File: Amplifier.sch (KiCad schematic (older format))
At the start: 49 parts, among them J501 Screw_Terminal_01x04, SW501 SW_DIP_x02, U501 TDA7498L

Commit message: fast alle footprints herausgesucht. Spulen typen rausgesucht: Bourns spulen
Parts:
- removed C525: 560uF 50V, Capacitor_THT:CP_Radial_D12.5mm_P5.00mm, symbol Device:CP
- added C530, C531, C532: 560uF 50V, Capacitor_THT:CP_Radial_D12.5mm_P5.00mm, symbol Device:CP_Small
- C525: renamed from C?; footprint (none) -> Capacitor_THT:CP_Radial_D13.0mm_P5.00mm
- C526, C527, C528, C529: footprint (none) -> Capacitor_SMD:C_0603_1608Metric_Pad1.05x0.95mm_HandSolder
- J501: value Screw_Terminal_01x04 -> TB001-500-04BE CUI_Devices; footprint (none) -> TerminalBlock_RND:TerminalBlock_RND_205-00047_1x04_P5.00mm_Horizontal
- L501, L502, L503, L504: value 22uH -> 22uH 6100-220K-RC
- R501, R502, R503, R504, R505, R512: footprint (none) -> Resistor_SMD:R_0603_1608Metric_Pad1.05x0.95mm_HandSolder
- R506, R507, R508, R509, R510, R511: footprint (none) -> Resistor_SMD:R_1206_3216Metric_Pad1.42x1.75mm_HandSolder
- SW501: value SW_DIP_x02 -> DS04-254-2-02BK-SMT; footprint (none) -> Package_DIP:DIP-4_W8.89mm_SMDSocket_LongPads
- U501: footprint (none) -> Package_SO:ST_PowerSSO-36_SlugDown_ThermalVias
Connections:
- net GNDPWR: now also C525.2, C530.2, C531.2, C532.2
- net POWER_AMP: now also C511.2, C512.1, C514.2, C515.1, C525.1, U501.12 (PVCCA), U501.13 (PVCCA), U501.6 (PVCCB), U501.7 (PVCCB), C530.1, C531.1, C532.1
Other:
- moved on the sheet: C525
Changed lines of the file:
@@
 F 0 "U501" H 5425 5415 50  0000 C CNN
 F 1 "TDA7498L" H 5425 5324 50  0000 C CNN
-F 2 "" H 5550 4250 50  0001 C CNN
+F 2 "Package_SO:ST_PowerSSO-36_SlugDown_ThermalVias" H 5550 4250 50  0001 C CNN
 F 3 "" H 5550 4250 50  0001 C CNN
 	1    5400 3650
@@
 F 0 "R506" H 6959 2446 50  0000 L CNN
 F 1 "22R" H 6959 2355 50  0000 L CNN
-F 2 "" H 6900 2400 50  0001 C CNN
+F 2 "Resistor_SMD:R_1206_3216Metric_Pad1.42x1.75mm_HandSolder" H 6900 2400 50  0001 C CNN
 F 3 "~" H 6900 2400 50  0001 C CNN
 	1    6900 2400
@@
 P 7300 2150
 F 0 "L501" V 7505 2150 50  0000 C CNN
-F 1 "22uH" V 7414 2150 50  0000 C CNN
+F 1 "22uH 6100-220K-RC " V 7414 2150 50  0000 C CNN
 F 2 "" H 7300 2150 50  0001 C CNN
 F 3 "~" H 7300 2150 50  0001 C CNN
@@
 P 7300 3300
 F 0 "L502" V 7505 3300 50  0000 C CNN
-F 1 "22uH" V 7414 3300 50  0000 C CNN
+F 1 "22uH 6100-220K-RC " V 7414 3300 50  0000 C CNN
 F 2 "" H 7300 3300 50  0001 C CNN
 F 3 "~" H 7300 3300 50  0001 C CNN
@@
 F 0 "R509" H 8509 3196 50  0000 L CNN
 F 1 "8R" H 8509 3105 50  0000 L CNN
-F 2 "" H 8450 3150 50  0001 C CNN
+F 2 "Resistor_SMD:R_1206_3216Metric_Pad1.42x1.75mm_HandSolder" H 8450 3150 50  0001 C CNN
 F 3 "~" H 8450 3150 50  0001 C CNN
 	1    8450 3150
@@
 F 0 "C527" H 8542 2946 50  0000 L CNN
 F 1 "220nF" H 8542 2855 50  0000 L CNN
-F 2 "" H 8450 2900 50  0001 C CNN
+F 2 "Capacitor_SMD:C_0603_1608Metric_Pad1.05x0.95mm_HandSolder" H 8450 2900 50  0001 C CNN
 F 3 "~" H 8450 2900 50  0001 C CNN
 	1    8450 2900
@@
 F 0 "R508" H 8509 2346 50  0000 L CNN
 F 1 "8R" H 8509 2255 50  0000 L CNN
-F 2 "" H 8450 2300 50  0001 C CNN
+F 2 "Resistor_SMD:R_1206_3216Metric_Pad1.42x1.75mm_HandSolder" H 8450 2300 50  0001 C CNN
 F 3 "~" H 8450 2300 50  0001 C CNN
 	1    8450 2300
@@
 F 0 "C526" H 8542 2596 50  0000 L CNN
 F 1 "220nF" H 8542 2505 50  0000 L CNN
-F 2 "" H 8450 2550 50  0001 C CNN
+F 2 "Capacitor_SMD:C_0603_1608Metric_Pad1.05x0.95mm_HandSolder" H 8450 2550 50  0001 C CNN
 F 3 "~" H 8450 2550 50  0001 C CNN
 	1    8450 2550
@@
 P 10300 3650
 F 0 "J501" H 10380 3642 50  0000 L CNN
-F 1 "Screw_Terminal_01x04" H 10380 3551 50  0000 L CNN
-F 2 "" H 10300 3650 50  0001 C CNN
+F 1 "TB001-500-04BE CUI_Devices" H 10000 3300 50  0000 L CNN
+F 2 "TerminalBlock_RND:TerminalBlock_RND_205-00047_1x04_P5.00mm_Horizontal" H 10300 3650 50  0001 C CNN
 F 3 "~" H 10300 3650 50  0001 C CNN
 	1    10300 3650
@@
 F 0 "R507" H 6959 4296 50  0000 L CNN
 F 1 "22R" H 6959 4205 50  0000 L CNN
-F 2 "" H 6900 4250 50  0001 C CNN
+F 2 "Resistor_SMD:R_1206_3216Metric_Pad1.42x1.75mm_HandSolder" H 6900 4250 50  0001 C CNN
 F 3 "~" H 6900 4250 50  0001 C CNN
 	1    6900 4250
@@
 P 7300 4000
 F 0 "L503" V 7505 4000 50  0000 C CNN
-F 1 "22uH" V 7414 4000 50  0000 C CNN
+F 1 "22uH 6100-220K-RC " V 7414 4000 50  0000 C CNN
 F 2 "" H 7300 4000 50  0001 C CNN
 F 3 "~" H 7300 4000 50  0001 C CNN
@@
 P 7300 5150
 F 0 "L504" V 7505 5150 50  0000 C CNN
-F 1 "22uH" V 7414 5150 50  0000 C CNN
+F 1 "22uH 6100-220K-RC " V 7414 5150 50  0000 C CNN
 F 2 "" H 7300 5150 50  0001 C CNN
 F 3 "~" H 7300 5150 50  0001 C CNN
@@
 F 0 "R511" H 8509 5046 50  0000 L CNN
 F 1 "8R" H 8509 4955 50  0000 L CNN
-F 2 "" H 8450 5000 50  0001 C CNN
+F 2 "Resistor_SMD:R_1206_3216Metric_Pad1.42x1.75mm_HandSolder" H 8450 5000 50  0001 C CNN
 F 3 "~" H 8450 5000 50  0001 C CNN
 	1    8450 5000
@@
 F 0 "C529" H 8542 4796 50  0000 L CNN
 F 1 "220nF" H 8542 4705 50  0000 L CNN
-F 2 "" H 8450 4750 50  0001 C CNN
+F 2 "Capacitor_SMD:C_0603_1608Metric_Pad1.05x0.95mm_HandSolder" H 8450 4750 50  0001 C CNN
 F 3 "~" H 8450 4750 50  0001 C CNN
 	1    8450 4750
@@
 F 0 "R510" H 8509 4196 50  0000 L CNN
 F 1 "8R" H 8509 4105 50  0000 L CNN
-F 2 "" H 8450 4150 50  0001 C CNN
+F 2 "Resistor_SMD:R_1206_3216Metric_Pad1.42x1.75mm_HandSolder" H 8450 4150 50  0001 C CNN
 F 3 "~" H 8450 4150 50  0001 C CNN
 	1    8450 4150
@@
 F 0 "C528" H 8542 4446 50  0000 L CNN
 F 1 "220nF" H 8542 4355 50  0000 L CNN
-F 2 "" H 8450 4400 50  0001 C CNN
+F 2 "Capacitor_SMD:C_0603_1608Metric_Pad1.05x0.95mm_HandSolder" H 8450 4400 50  0001 C CNN
 F 3 "~" H 8450 4400 50  0001 C CNN
 	1    8450 4400
@@
 Text GLabel 9350 3500 2    50   Input ~ 0
 POWER_AMP
-$Comp
-L Device:CP C525
-U 1 1 5E78AA8C
-P 8250 3650
-F 0 "C525" H 8368 3696 50  0000 L CNN
-F 1 "560uF 50V" H 8368 3605 50  0000 L CNN
-F 2 "Capacitor_THT:CP_Radial_D12.5mm_P5.00mm" H 8288 3500 50  0001 C CNN
-F 3 "~" H 8250 3650 50  0001 C CNN
-	1    8250 3650
-	1    0    0    -1
-$EndComp
-Wire Wire Line
-	8750 3500 8250 3500
-Wire Wire Line
-	8250 3500 6500 3500
-Connection ~ 8250 3500
 Connection ~ 6500 3500
 Wire Wire Line
@@
 F 0 "R505" V 3504 3000 50  0000 C CNN
 F 1 "100k" V 3595 3000 50  0000 C CNN
-F 2 "" H 3700 3000 50  0001 C CNN
+F 2 "Resistor_SMD:R_0603_1608Metric_Pad1.05x0.95mm_HandSolder" H 3700 3000 50  0001 C CNN
 F 3 "~" H 3700 3000 50  0001 C CNN
 	1    3700 3000
@@
 F 0 "R503" H 3800 3050 50  0000 R CNN
 F 1 "22R" H 3800 3150 50  0000 R CNN
-F 2 "" H 3500 3100 50  0001 C CNN
+F 2 "Resistor_SMD:R_0603_1608Metric_Pad1.05x0.95mm_HandSolder" H 3500 3100 50  0001 C CNN
 F 3 "~" H 3500 3100 50  0001 C CNN
 	1    3500 3100
@@
 F 0 "R504" H 3700 4000 50  0000 R CNN
 F 1 "39K" H 3700 4100 50  0000 R CNN
-F 2 "" H 3500 4050 50  0001 C CNN
+F 2 "Resistor_SMD:R_0603_1608Metric_Pad1.05x0.95mm_HandSolder" H 3500 4050 50  0001 C CNN
 F 3 "~" H 3500 4050 50  0001 C CNN
 	1    3500 4050
@@
 F 0 "R502" V 3100 5650 50  0000 C CNN
 F 1 "47K" V 3200 5700 50  0000 C CNN
-F 2 "" H 3000 5700 50  0001 C CNN
+F 2 "Resistor_SMD:R_0603_1608Metric_Pad1.05x0.95mm_HandSolder" H 3000 5700 50  0001 C CNN
 F 3 "~" H 3000 5700 50  0001 C CNN
 	1    3000 5700
@@
 F 0 "R501" V 2804 5550 50  0000 C CNN
 F 1 "47K" V 2895 5550 50  0000 C CNN
-F 2 "" H 3000 5550 50  0001 C CNN
+F 2 "Resistor_SMD:R_0603_1608Metric_Pad1.05x0.95mm_HandSolder" H 3000 5550 50  0001 C CNN
 F 3 "~" H 3000 5550 50  0001 C CNN
 	1    3000 5550
@@
 P 4300 4100
 F 0 "SW501" H 4300 4467 50  0000 C CNN
-F 1 "SW_DIP_x02" H 4300 4376 50  0000 C CNN
-F 2 "" H 4300 4100 50  0001 C CNN
+F 1 "DS04-254-2-02BK-SMT" H 4300 4376 50  0000 C CNN
+F 2 "Package_DIP:DIP-4_W8.89mm_SMDSocket_LongPads" H 4300 4100 50  0001 C CNN
 F 3 "" H 4300 4100 50  0001 C CNN
 	1    4300 4100
@@
 L power:GNDPWR #PWR0505
 U 1 1 5E90BDCB
-P 8250 3800
-F 0 "#PWR0505" H 8250 3600 50  0001 C CNN
-F 1 "GNDPWR" H 8500 3750 50  0000 C CNN
-F 2 "" H 8250 3750 50  0001 C CNN
-F 3 "" H 8250 3750 50  0001 C CNN
-	1    8250 3800
+P 9050 3800
+F 0 "#PWR0505" H 9050 3600 50  0001 C CNN
+F 1 "GNDPWR" H 9300 3750 50  0000 C CNN
+F 2 "" H 9050 3750 50  0001 C CNN
+F 3 "" H 9050 3750 50  0001 C CNN
+	1    9050 3800
 	1    0    0    -1
 $EndComp
@@
 F 0 "R512" V 7804 3800 50  0000 C CNN
 F 1 "0R" V 7895 3800 50  0000 C CNN
-F 2 "" H 8000 3800 50  0001 C CNN
+F 2 "Resistor_SMD:R_0603_1608Metric_Pad1.05x0.95mm_HandSolder" H 8000 3800 50  0001 C CNN
 F 3 "~" H 8000 3800 50  0001 C CNN
 	1    8000 3800
@@
 Wire Wire Line
 	8100 3800 8250 3800
-Connection ~ 8250 3800
 $Comp
 L power:GNDS #PWR0179
@@
 Connection ~ 7700 3800
 $Comp
-L Device:CP_Small C?
+L Device:CP_Small C525
 U 1 1 5EC3CBA6
-P 9050 3700
-F 0 "C?" H 9138 3746 50  0000 L CNN
-F 1 "560uF 50V" H 9138 3655 50  0000 L CNN
-F 2 "" H 9050 3700 50  0001 C CNN
-F 3 "~" H 9050 3700 50  0001 C CNN
-	1    9050 3700
-	1    0    0    -1
-$EndComp
+P 8250 3600
+F 0 "C525" H 8338 3646 50  0000 L CNN
+F 1 "560uF 50V" H 8050 3750 50  0000 L CNN
+F 2 "Capacitor_THT:CP_Radial_D13.0mm_P5.00mm" H 8250 3600 50  0001 C CNN
+F 3 "~" H 8250 3600 50  0001 C CNN
+	1    8250 3600
+	1    0    0    -1
+$EndComp
+Wire Wire Line
+	6500 3500 8250 3500
+Connection ~ 8250 3500
+Wire Wire Line
+	8250 3500 8550 3500
+$Comp
+L Device:CP_Small C530
+U 1 1 5EC3DA10
+P 8550 3600
+F 0 "C530" H 8638 3646 50  0000 L CNN
+F 1 "560uF 50V" H 8450 3800 50  0000 L CNN
+F 2 "Capacitor_THT:CP_Radial_D12.5mm_P5.00mm" H 8550 3600 50  0001 C CNN
+F 3 "~" H 8550 3600 50  0001 C CNN
+	1    8550 3600
+	1    0    0    -1
+$EndComp
+Connection ~ 8550 3500
+$Comp
+L Device:CP_Small C531
+U 1 1 5EC3DE15
+P 8800 3600
+F 0 "C531" H 8888 3646 50  0000 L CNN
+F 1 "560uF 50V" H 8700 3800 50  0000 L CNN
+F 2 "Capacitor_THT:CP_Radial_D12.5mm_P5.00mm" H 8800 3600 50  0001 C CNN
+F 3 "~" H 8800 3600 50  0001 C CNN
+	1    8800 3600
+	1    0    0    -1
+$EndComp
+$Comp
+L Device:CP_Small C532
+U 1 1 5EC3DE8F
+P 9050 3600
+F 0 "C532" H 9138 3646 50  0000 L CNN
+F 1 "560uF 50V" H 8950 3800 50  0000 L CNN
+F 2 "Capacitor_THT:CP_Radial_D12.5mm_P5.00mm" H 9050 3600 50  0001 C CNN
+F 3 "~" H 9050 3600 50  0001 C CNN
+	1    9050 3600
+	1    0    0    -1
+$EndComp
+Wire Wire Line
+	8550 3500 8800 3500
+Connection ~ 8800 3500
+Wire Wire Line
+	8800 3500 9050 3500
+Wire Wire Line
+	9050 3800 9050 3700
+Wire Wire Line
+	8250 3700 8250 3800
+Wire Wire Line
+	8550 3700 8550 3800
+Wire Wire Line
+	8550 3800 8800 3800
+Connection ~ 9050 3800
+Wire Wire Line
+	8800 3700 8800 3800
+Connection ~ 8800 3800
+Wire Wire Line
+	8800 3800 9050 3800
+Wire Wire Line
+	8250 3800 8550 3800
+Connection ~ 8250 3800
+Connection ~ 8550 3800
+Wire Wire Line
+	9350 3500 9050 3500
+Connection ~ 9050 3500
 $EndSCHEMATC

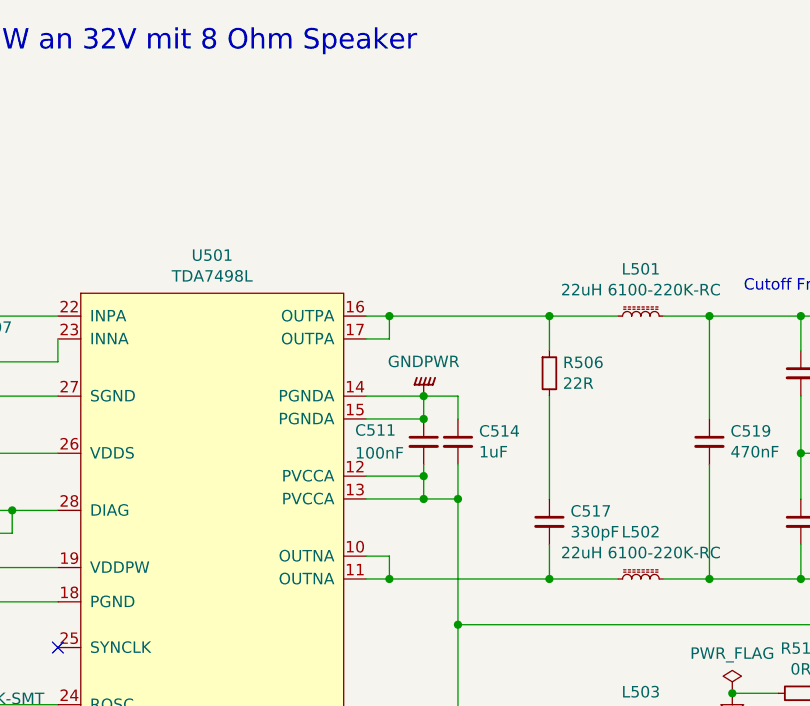
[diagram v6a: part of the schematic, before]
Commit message: Port Expander und Rotary Encoder hinzugefügt. TODO: Footprint Heatsink Amp
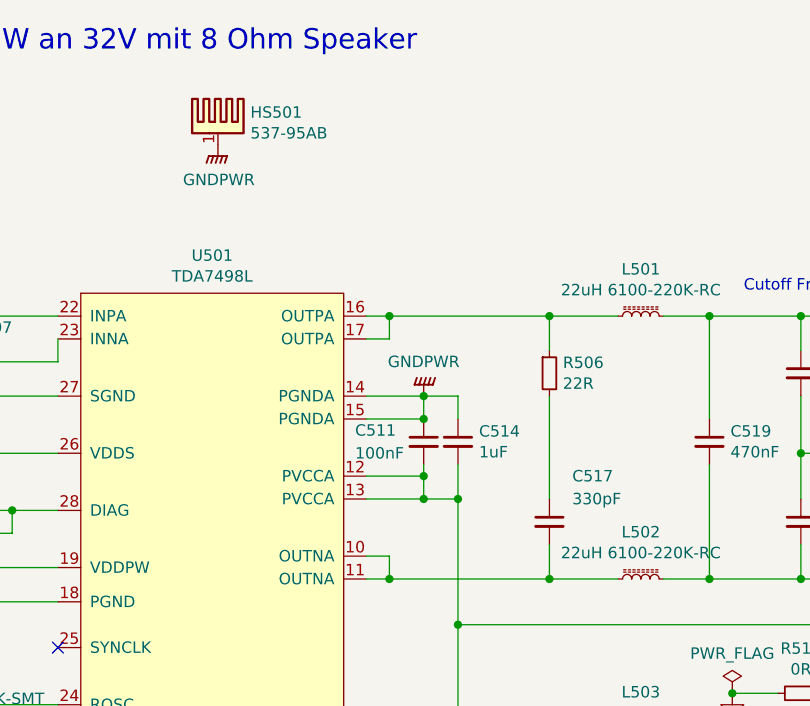
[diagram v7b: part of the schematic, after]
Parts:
- added HS501: 537-95AB, symbol Mechanical:Heatsink_Pad
- L501, L502, L503, L504: footprint (none) -> Inductor_THT:L_Radial_D12.0mm_P6.00mm_MuRATA_1900R
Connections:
- net GNDPWR: now also HS501.1
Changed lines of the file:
@@
 $Descr A4 11693 8268
 encoding utf-8
-Sheet 5 7
+Sheet 5 8
 Title ""
 Date ""
@@
 F 1 "TDA7498L" H 5425 5324 50  0000 C CNN
 F 2 "Package_SO:ST_PowerSSO-36_SlugDown_ThermalVias" H 5550 4250 50  0001 C CNN
-F 3 "" H 5550 4250 50  0001 C CNN
+F 3 "/home/niko/kicad/datasheet/TDA7498L.pdf" H 5550 4250 50  0001 C CNN
 	1    5400 3650
 	1    0    0    -1
@@
 F 0 "L501" V 7505 2150 50  0000 C CNN
 F 1 "22uH 6100-220K-RC " V 7414 2150 50  0000 C CNN
-F 2 "" H 7300 2150 50  0001 C CNN
-F 3 "~" H 7300 2150 50  0001 C CNN
+F 2 "Inductor_THT:L_Radial_D12.0mm_P6.00mm_MuRATA_1900R" H 7300 2150 50  0001 C CNN
+F 3 "https://www.mouser.de/datasheet/2/54/6100_series-776994.pdf" H 7300 2150 50  0001 C CNN
 	1    7300 2150
 	0    -1   -1   0
@@
 U 1 1 5E758E07
 P 6900 3050
-F 0 "C517" H 6992 3096 50  0000 L CNN
-F 1 "330pF" H 6992 3005 50  0000 L CNN
+F 0 "C517" H 7000 3250 50  0000 L CNN
+F 1 "330pF" H 7000 3150 50  0000 L CNN
 F 2 "Capacitor_SMD:C_0603_1608Metric_Pad1.05x0.95mm_HandSolder" H 6900 3050 50  0001 C CNN
 F 3 "~" H 6900 3050 50  0001 C CNN
@@
 F 0 "L502" V 7505 3300 50  0000 C CNN
 F 1 "22uH 6100-220K-RC " V 7414 3300 50  0000 C CNN
-F 2 "" H 7300 3300 50  0001 C CNN
-F 3 "~" H 7300 3300 50  0001 C CNN
+F 2 "Inductor_THT:L_Radial_D12.0mm_P6.00mm_MuRATA_1900R" H 7300 3300 50  0001 C CNN
+F 3 "https://www.mouser.de/datasheet/2/54/6100_series-776994.pdf" H 7300 3300 50  0001 C CNN
 	1    7300 3300
 	0    -1   -1   0
@@
 F 0 "L503" V 7505 4000 50  0000 C CNN
 F 1 "22uH 6100-220K-RC " V 7414 4000 50  0000 C CNN
-F 2 "" H 7300 4000 50  0001 C CNN
-F 3 "~" H 7300 4000 50  0001 C CNN
+F 2 "Inductor_THT:L_Radial_D12.0mm_P6.00mm_MuRATA_1900R" H 7300 4000 50  0001 C CNN
+F 3 "https://www.mouser.de/datasheet/2/54/6100_series-776994.pdf" H 7300 4000 50  0001 C CNN
 	1    7300 4000
 	0    -1   -1   0
@@
 F 0 "L504" V 7505 5150 50  0000 C CNN
 F 1 "22uH 6100-220K-RC " V 7414 5150 50  0000 C CNN
-F 2 "" H 7300 5150 50  0001 C CNN
-F 3 "~" H 7300 5150 50  0001 C CNN
+F 2 "Inductor_THT:L_Radial_D12.0mm_P6.00mm_MuRATA_1900R" H 7300 5150 50  0001 C CNN
+F 3 "https://www.mouser.de/datasheet/2/54/6100_series-776994.pdf" H 7300 5150 50  0001 C CNN
 	1    7300 5150
 	0    -1   -1   0
@@
 F 1 "DS04-254-2-02BK-SMT" H 4300 4376 50  0000 C CNN
 F 2 "Package_DIP:DIP-4_W8.89mm_SMDSocket_LongPads" H 4300 4100 50  0001 C CNN
-F 3 "" H 4300 4100 50  0001 C CNN
+F 3 "https://www.mouser.de/datasheet/2/670/ds04-254-smt-1777718.pdf" H 4300 4100 50  0001 C CNN
 	1    4300 4100
 	1    0    0    -1
@@
 F 1 "560uF 50V" H 8050 3750 50  0000 L CNN
 F 2 "Capacitor_THT:CP_Radial_D13.0mm_P5.00mm" H 8250 3600 50  0001 C CNN
-F 3 "~" H 8250 3600 50  0001 C CNN
+F 3 "https://www.mouser.de/datasheet/2/420/United-Chemi-Con-1109128.pdf" H 8250 3600 50  0001 C CNN
 	1    8250 3600
 	1    0    0    -1
@@
 F 1 "560uF 50V" H 8450 3800 50  0000 L CNN
 F 2 "Capacitor_THT:CP_Radial_D12.5mm_P5.00mm" H 8550 3600 50  0001 C CNN
-F 3 "~" H 8550 3600 50  0001 C CNN
+F 3 "https://www.mouser.de/datasheet/2/420/United-Chemi-Con-1109128.pdf" H 8550 3600 50  0001 C CNN
 	1    8550 3600
 	1    0    0    -1
@@
 F 1 "560uF 50V" H 8700 3800 50  0000 L CNN
 F 2 "Capacitor_THT:CP_Radial_D12.5mm_P5.00mm" H 8800 3600 50  0001 C CNN
-F 3 "~" H 8800 3600 50  0001 C CNN
+F 3 "https://www.mouser.de/datasheet/2/420/United-Chemi-Con-1109128.pdf" H 8800 3600 50  0001 C CNN
 	1    8800 3600
 	1    0    0    -1
@@
 F 1 "560uF 50V" H 8950 3800 50  0000 L CNN
 F 2 "Capacitor_THT:CP_Radial_D12.5mm_P5.00mm" H 9050 3600 50  0001 C CNN
-F 3 "~" H 9050 3600 50  0001 C CNN
+F 3 "https://www.mouser.de/datasheet/2/420/United-Chemi-Con-1109128.pdf" H 9050 3600 50  0001 C CNN
 	1    9050 3600
 	1    0    0    -1
@@
 	9350 3500 9050 3500
 Connection ~ 9050 3500
+$Comp
+L Mechanical:Heatsink_Pad HS501
+U 1 1 5F733287
+P 5450 1300
+F 0 "HS501" H 5592 1341 50  0000 L CNN
+F 1 "537-95AB" H 5592 1250 50  0000 L CNN
+F 2 "" H 5462 1250 50  0001 C CNN
+F 3 "https://www.mouser.de/datasheet/2/433/extruded-heat-sink-wakefield-365172.pdf" H 5462 1250 50  0001 C CNN
+	1    5450 1300
+	1    0    0    -1
+$EndComp
+$Comp
+L power:GNDPWR #PWR0501
+U 1 1 5F7336DD
+P 5450 1400
+F 0 "#PWR0501" H 5450 1200 50  0001 C CNN
+F 1 "GNDPWR" H 5454 1246 50  0000 C CNN
+F 2 "" H 5450 1350 50  0001 C CNN
+F 3 "" H 5450 1350 50  0001 C CNN
+	1    5450 1400
+	1    0    0    -1
+$EndComp
 $EndSCHEMATC

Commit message: PCB angefangen: Charger geplaced
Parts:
- HS501: footprint (none) -> Heatsink:Heatsink_57.9x36.8mm_4xFixation3.17mm_537-95AB
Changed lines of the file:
@@
 F 0 "HS501" H 5592 1341 50  0000 L CNN
 F 1 "537-95AB" H 5592 1250 50  0000 L CNN
-F 2 "" H 5462 1250 50  0001 C CNN
+F 2 "Heatsink:Heatsink_57.9x36.8mm_4xFixation3.17mm_537-95AB" H 5462 1250 50  0001 C CNN
 F 3 "https://www.mouser.de/datasheet/2/433/extruded-heat-sink-wakefield-365172.pdf" H 5462 1250 50  0001 C CNN
 	1    5450 1300
